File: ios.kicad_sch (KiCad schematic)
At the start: 42 parts, among them Q4 BSS138PW,115, SW1 SW_SKRPABE010, SW2 SW_SKRPABE010, SW3 SW_SKRPABE010, SW4 SW_SKRPABE010, SW8 CVS-04B, U25 74LVC06ABQ

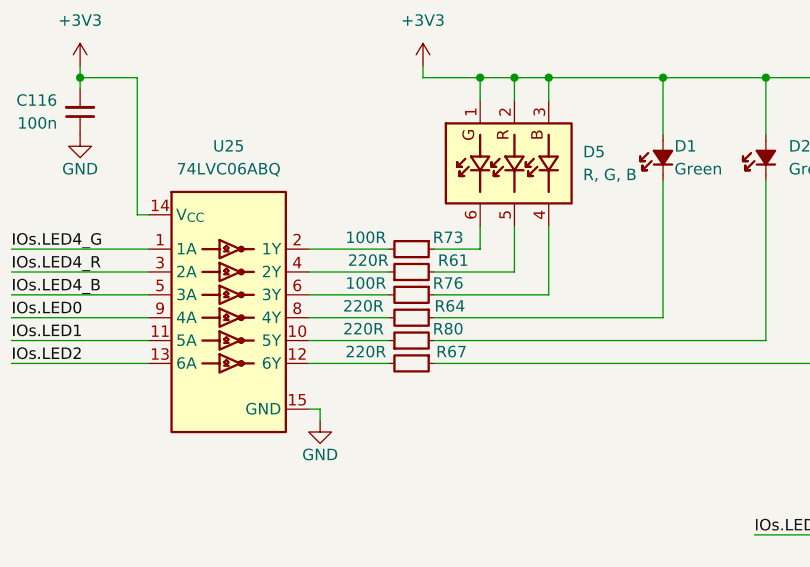
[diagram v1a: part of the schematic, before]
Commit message: [#98576] Replace RGB LED resistors with 1k
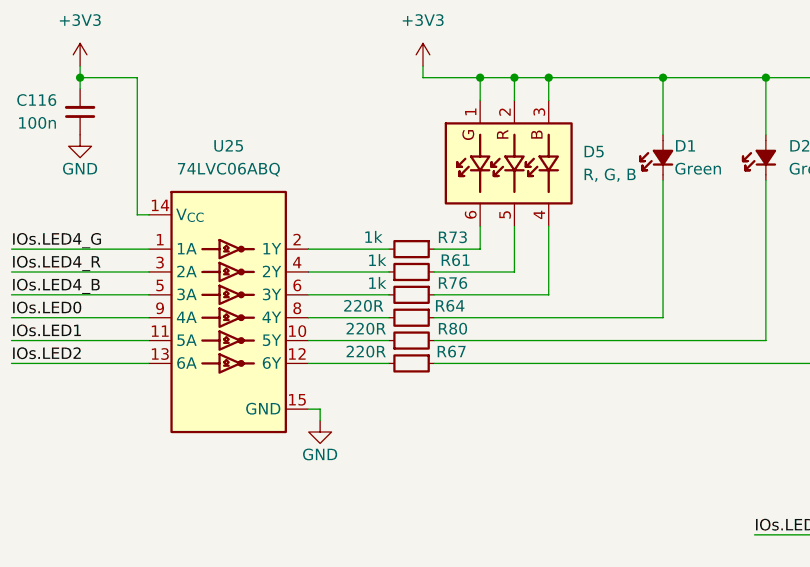
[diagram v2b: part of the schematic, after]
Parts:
- R61: value R_220R_0402 -> R_1k_0402; symbol antmicroResistors0402:R_220R_0402 -> antmicroResistors0402:R_1k_0402; MPN CR0402-FX-2200GLF -> CR0402-FX-1001GLF; Val 220R -> 1k
- R73, R76: value R_100R_0402 -> R_1k_0402; symbol antmicroResistors0402:R_100R_0402 -> antmicroResistors0402:R_1k_0402; MPN CR0402-FX-1000GLF -> CR0402-FX-1001GLF; Val 100R -> 1k
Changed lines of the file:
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@@
 	)
 	(symbol
-		(lib_id "antmicroResistors0402:R_100R_0402")
+		(lib_id "antmicroResistors0402:R_1k_0402")
 		(at 151.13 86.36 0)
 		(mirror y)
@@
 		(dnp no)
 		(property "Reference" "R73"
-			(at 152.654 85.09 0)
+			(at 153.162 85.09 0)
 			(effects
 				(font
@@
 			)
 		)
-		(property "Value" "R_100R_0402"
+		(property "Value" "R_1k_0402"
 			(at 130.81 99.06 0)
 			(effects
@@
 			)
 		)
-		(property "Description" "SMD Chip Resistor, 100 ohm, ± 1%, 62.5 mW, 0402 [1005 Metric], Thick Film, General Purpose"
+		(property "Description" "SMD Chip Resistor, 1 kohm, ± 1%, 63 mW, 0402 [1005 Metric], Thick Film, General Purpose"
 			(at 130.81 116.84 0)
 			(effects
@@
 			)
 		)
-		(property "MPN" "CR0402-FX-1000GLF"
+		(property "MPN" "CR0402-FX-1001GLF"
 			(at 130.81 106.68 0)
 			(effects
@@
 			)
 		)
-		(property "Val" "100R"
-			(at 143.51 85.09 0)
+		(property "Val" "1k"
+			(at 145.796 88.392 0)
 			(effects
 				(font
@@
 					(thickness 0.15)
 				)
+				(justify left bottom)
 			)
 		)
@@
 	)
 	(symbol
-		(lib_id "antmicroResistors0402:R_100R_0402")
+		(lib_id "antmicroResistors0402:R_1k_0402")
 		(at 151.13 91.44 0)
 		(mirror y)
@@
 		(dnp no)
 		(property "Reference" "R76"
-			(at 152.654 90.17 0)
+			(at 153.162 90.17 0)
 			(effects
 				(font
@@
 			)
 		)
-		(property "Value" "R_100R_0402"
+		(property "Value" "R_1k_0402"
 			(at 130.81 104.14 0)
 			(effects
@@
 			)
 		)
-		(property "Description" "SMD Chip Resistor, 100 ohm, ± 1%, 62.5 mW, 0402 [1005 Metric], Thick Film, General Purpose"
+		(property "Description" "SMD Chip Resistor, 1 kohm, ± 1%, 63 mW, 0402 [1005 Metric], Thick Film, General Purpose"
 			(at 130.81 121.92 0)
 			(effects
@@
 			)
 		)
-		(property "MPN" "CR0402-FX-1000GLF"
+		(property "MPN" "CR0402-FX-1001GLF"
 			(at 130.81 111.76 0)
 			(effects
@@
 			)
 		)
-		(property "Val" "100R"
-			(at 143.51 90.17 0)
+		(property "Val" "1k"
+			(at 145.796 90.932 0)
 			(effects
 				(font
@@
 					(thickness 0.15)
 				)
+				(justify left bottom)
 			)
 		)
@@
 	)
 	(symbol
-		(lib_id "antmicroResistors0402:R_220R_0402")
+		(lib_id "antmicroResistors0402:R_1k_0402")
 		(at 146.05 88.9 0)
 		(mirror x)
@@
 		(dnp no)
 		(property "Reference" "R61"
-			(at 154.94 87.63 0)
+			(at 155.194 87.63 0)
 			(effects
 				(font
@@
 			)
 		)
-		(property "Value" "R_220R_0402"
+		(property "Value" "R_1k_0402"
 			(at 166.37 76.2 0)
 			(effects
@@
 			)
 		)
-		(property "Description" "SMD Chip Resistor, 220 ohm, ± 1%, 62.5 mW, 0402 [1005 Metric], Thick Film, General Purpose"
+		(property "Description" "SMD Chip Resistor, 1 kohm, ± 1%, 63 mW, 0402 [1005 Metric], Thick Film, General Purpose"
 			(at 166.37 58.42 0)
 			(effects
@@
 			)
 		)
-		(property "MPN" "CR0402-FX-2200GLF"
+		(property "MPN" "CR0402-FX-1001GLF"
 			(at 166.37 68.58 0)
 			(effects
@@
 			)
 		)
-		(property "Val" "220R"
-			(at 146.05 87.63 0)
+		(property "Val" "1k"
+			(at 143.256 84.328 0)
 			(effects
 				(font
@@
 					(thickness 0.15)
 				)
-				(justify right)
+				(justify left bottom)
 			)
 		)
@@
 		(dnp no)
 		(property "Reference" "R80"
-			(at 152.654 95.25 0)
+			(at 153.162 95.25 0)
 			(effects
 				(font
@@
 		)
 		(property "Val" "220R"
-			(at 143.256 95.25 0)
+			(at 143.51 95.25 0)
 			(effects
 				(font

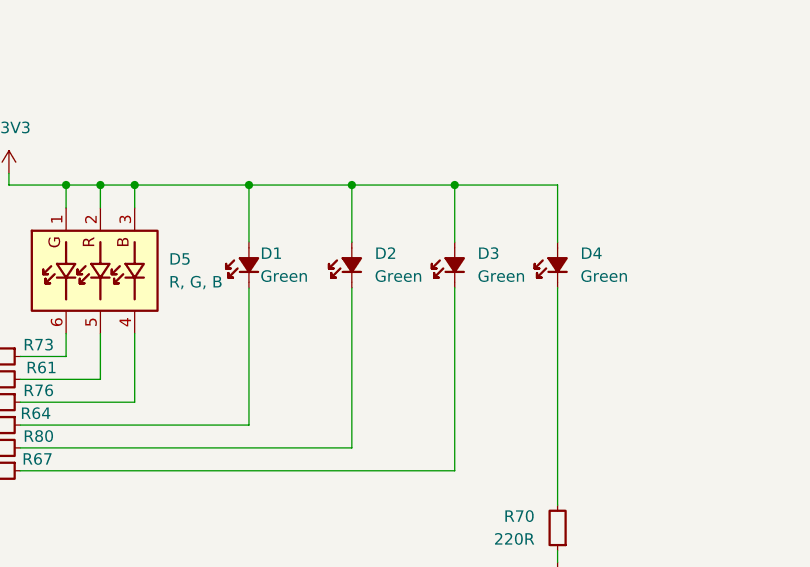
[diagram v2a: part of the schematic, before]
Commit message: [#98577] Unify LEDs
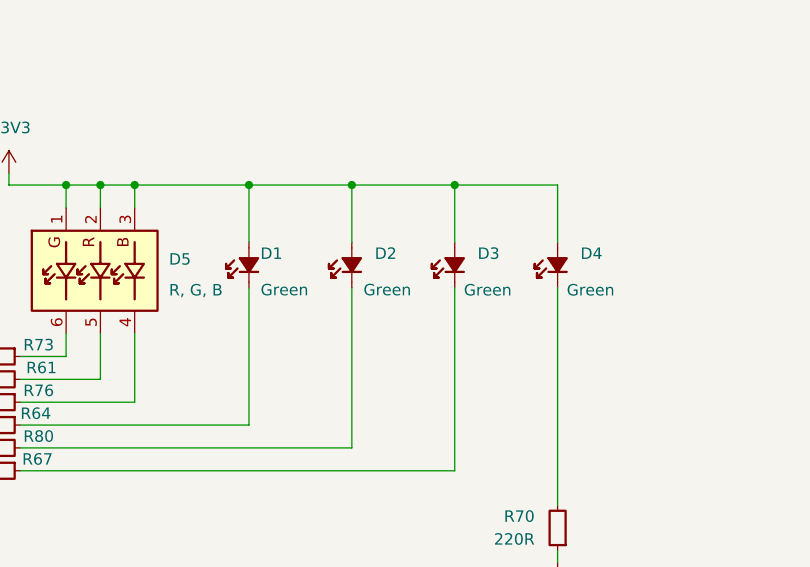
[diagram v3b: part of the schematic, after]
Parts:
- D1, D2, D3, D4: value LED_G_0402_VLMTG1500-GS08 -> LED_G_0603_LG_L29K-G2J1-24-Z; footprint antmicro-footprints:LED_0402_1005Metric_G -> antmicro-footprints:LED_0603_1608Metric_G; symbol antmicroLEDIndicationDiscrete:LED_G_0402_VLMTG1500-GS08 -> antmicroLEDIndicationDiscrete:LED_G_0603_LG_L29K-G2J1-24-Z; MPN VLMTG1500-GS08 -> LG L29K-G2J1-24-Z; Manufacturer Vishay -> OSRAM
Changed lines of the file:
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@@
 	)
 	(symbol
-		(lib_id "antmicroLEDIndicationDiscrete:LED_G_0402_VLMTG1500-GS08")
+		(lib_id "antmicroLEDIndicationDiscrete:LED_G_0603_LG_L29K-G2J1-24-Z")
 		(at 176.53 78.74 90)
 		(unit 1)
@@
 			)
 		)
-		(property "Value" "LED_G_0402_VLMTG1500-GS08"
-			(at 184.15 55.88 0)
+		(property "Value" "LED_G_0603_LG_L29K-G2J1-24-Z"
+			(at 184.15 58.42 0)
 			(effects
 				(font
@@
 			)
 		)
-		(property "Footprint" "antmicro-footprints:LED_0402_1005Metric_G"
-			(at 186.69 55.88 0)
+		(property "Footprint" "antmicro-footprints:LED_0603_1608Metric_G"
+			(at 186.69 58.42 0)
 			(effects
 				(font
@@
 			)
 		)
-		(property "Datasheet" "https://www.vishay.com/docs/82554/vlmo1500.pdf"
-			(at 189.23 55.88 0)
+		(property "Datasheet" "https://look.ams-osram.com/m/19ee86b3ae0ee95b/original/LG-L29K.pdf"
+			(at 189.23 58.42 0)
 			(effects
 				(font
@@
 			)
 		)
-		(property "Description" "LED, Green, SMD, 1005, 5 mA, 3.1 V, 535 nm"
-			(at 201.93 55.88 0)
+		(property "Description" "LED, Green, SMD, 0603, 20 mA, 1.7 V, 570 nm"
+			(at 201.93 58.42 0)
 			(effects
 				(font
@@
 			)
 		)
-		(property "MPN" "VLMTG1500-GS08"
-			(at 191.77 55.88 0)
+		(property "MPN" "LG L29K-G2J1-24-Z"
+			(at 191.77 58.42 0)
 			(effects
 				(font
@@
 			)
 		)
-		(property "Manufacturer" "Vishay"
-			(at 194.31 55.88 0)
+		(property "Manufacturer" "OSRAM"
+			(at 194.31 58.42 0)
 			(effects
 				(font
@@
 		)
 		(property "Color" "Green"
-			(at 177.8 77.4699 90)
+			(at 183.134 78.232 90)
 			(effects
 				(font
 					(size 1.27 1.27)
 				)
-				(justify right)
+				(justify left bottom)
 			)
 		)
 		(property "Author" "Antmicro"
-			(at 196.85 55.88 0)
+			(at 196.85 58.42 0)
 			(effects
 				(font
@@
 		)
 		(property "License" "Apache-2.0"
-			(at 199.39 55.88 0)
+			(at 199.39 58.42 0)
 			(effects
 				(font
@@
 	)
 	(symbol
-		(lib_id "antmicroLEDIndicationDiscrete:LED_G_0402_VLMTG1500-GS08")
+		(lib_id "antmicroLEDIndicationDiscrete:LED_G_0603_LG_L29K-G2J1-24-Z")
 		(at 199.39 78.74 90)
 		(unit 1)
@@
 		(on_board yes)
 		(dnp no)
-		(fields_autoplaced yes)
 		(property "Reference" "D3"
 			(at 201.93 74.93 90)
@@
 			)
 		)
-		(property "Value" "LED_G_0402_VLMTG1500-GS08"
-			(at 207.01 55.88 0)
+		(property "Value" "LED_G_0603_LG_L29K-G2J1-24-Z"
+			(at 207.01 58.42 0)
 			(effects
 				(font
@@
 			)
 		)
-		(property "Footprint" "antmicro-footprints:LED_0402_1005Metric_G"
-			(at 209.55 55.88 0)
+		(property "Footprint" "antmicro-footprints:LED_0603_1608Metric_G"
+			(at 209.55 58.42 0)
 			(effects
 				(font
@@
 			)
 		)
-		(property "Datasheet" "https://www.vishay.com/docs/82554/vlmo1500.pdf"
-			(at 212.09 55.88 0)
+		(property "Datasheet" "https://look.ams-osram.com/m/19ee86b3ae0ee95b/original/LG-L29K.pdf"
+			(at 212.09 58.42 0)
 			(effects
 				(font
@@
 			)
 		)
-		(property "Description" "LED, Green, SMD, 1005, 5 mA, 3.1 V, 535 nm"
-			(at 224.79 55.88 0)
+		(property "Description" "LED, Green, SMD, 0603, 20 mA, 1.7 V, 570 nm"
+			(at 224.79 58.42 0)
 			(effects
 				(font
@@
 			)
 		)
-		(property "MPN" "VLMTG1500-GS08"
-			(at 214.63 55.88 0)
+		(property "MPN" "LG L29K-G2J1-24-Z"
+			(at 214.63 58.42 0)
 			(effects
 				(font
@@
 			)
 		)
-		(property "Manufacturer" "Vishay"
-			(at 217.17 55.88 0)
+		(property "Manufacturer" "OSRAM"
+			(at 217.17 58.42 0)
 			(effects
 				(font
@@
 		)
 		(property "Color" "Green"
-			(at 201.93 77.4699 90)
+			(at 200.406 78.994 90)
 			(effects
 				(font
@@
 		)
 		(property "Author" "Antmicro"
-			(at 219.71 55.88 0)
+			(at 219.71 58.42 0)
 			(effects
 				(font
@@
 		)
 		(property "License" "Apache-2.0"
-			(at 222.25 55.88 0)
+			(at 222.25 58.42 0)
 			(effects
 				(font
@@
 	)
 	(symbol
-		(lib_id "antmicroLEDIndicationDiscrete:LED_G_0402_VLMTG1500-GS08")
+		(lib_id "antmicroLEDIndicationDiscrete:LED_G_0603_LG_L29K-G2J1-24-Z")
 		(at 187.96 78.74 90)
 		(unit 1)
@@
 			)
 		)
-		(property "Value" "LED_G_0402_VLMTG1500-GS08"
-			(at 195.58 55.88 0)
+		(property "Value" "LED_G_0603_LG_L29K-G2J1-24-Z"
+			(at 195.58 58.42 0)
 			(effects
 				(font
@@
 			)
 		)
-		(property "Footprint" "antmicro-footprints:LED_0402_1005Metric_G"
-			(at 198.12 55.88 0)
+		(property "Footprint" "antmicro-footprints:LED_0603_1608Metric_G"
+			(at 198.12 58.42 0)
 			(effects
 				(font
@@
 			)
 		)
-		(property "Datasheet" "https://www.vishay.com/docs/82554/vlmo1500.pdf"
-			(at 200.66 55.88 0)
+		(property "Datasheet" "https://look.ams-osram.com/m/19ee86b3ae0ee95b/original/LG-L29K.pdf"
+			(at 200.66 58.42 0)
 			(effects
 				(font
@@
 			)
 		)
-		(property "Description" "LED, Green, SMD, 1005, 5 mA, 3.1 V, 535 nm"
-			(at 213.36 55.88 0)
+		(property "Description" "LED, Green, SMD, 0603, 20 mA, 1.7 V, 570 nm"
+			(at 213.36 58.42 0)
 			(effects
 				(font
@@
 			)
 		)
-		(property "MPN" "VLMTG1500-GS08"
-			(at 203.2 55.88 0)
+		(property "MPN" "LG L29K-G2J1-24-Z"
+			(at 203.2 58.42 0)
 			(effects
 				(font
@@
 			)
 		)
-		(property "Manufacturer" "Vishay"
-			(at 205.74 55.88 0)
+		(property "Manufacturer" "OSRAM"
+			(at 205.74 58.42 0)
 			(effects
 				(font
@@
 		)
 		(property "Color" "Green"
-			(at 190.5 77.4699 90)
+			(at 194.564 78.232 90)
 			(effects
 				(font
 					(size 1.27 1.27)
 				)
-				(justify right)
+				(justify left bottom)
 			)
 		)
 		(property "Author" "Antmicro"
-			(at 208.28 55.88 0)
+			(at 208.28 58.42 0)
 			(effects
 				(font
@@
 		)
 		(property "License" "Apache-2.0"
-			(at 210.82 55.88 0)
+			(at 210.82 58.42 0)
 			(effects
 				(font
@@
 		(on_board yes)
 		(dnp no)
-		(fields_autoplaced yes)
 		(property "Reference" "D5"
 			(at 167.64 75.565 90)
@@
 		)
 		(property "Color" "R, G, B"
-			(at 167.64 78.1049 90)
+			(at 167.64 78.994 90)
 			(effects
 				(font
@@
 	)
 	(symbol
-		(lib_id "antmicroLEDIndicationDiscrete:LED_G_0402_VLMTG1500-GS08")
+		(lib_id "antmicroLEDIndicationDiscrete:LED_G_0603_LG_L29K-G2J1-24-Z")
 		(at 210.82 78.74 90)
 		(unit 1)
@@
 		(on_board yes)
 		(dnp no)
-		(fields_autoplaced yes)
 		(property "Reference" "D4"
 			(at 213.36 74.93 90)
@@
 			)
 		)
-		(property "Value" "LED_G_0402_VLMTG1500-GS08"
-			(at 218.44 55.88 0)
+		(property "Value" "LED_G_0603_LG_L29K-G2J1-24-Z"
+			(at 218.44 58.42 0)
 			(effects
 				(font
@@
 			)
 		)
-		(property "Footprint" "antmicro-footprints:LED_0402_1005Metric_G"
-			(at 220.98 55.88 0)
+		(property "Footprint" "antmicro-footprints:LED_0603_1608Metric_G"
+			(at 220.98 58.42 0)
 			(effects
 				(font
@@
 			)
 		)
-		(property "Datasheet" "https://www.vishay.com/docs/82554/vlmo1500.pdf"
-			(at 223.52 55.88 0)
+		(property "Datasheet" "https://look.ams-osram.com/m/19ee86b3ae0ee95b/original/LG-L29K.pdf"
+			(at 223.52 58.42 0)
 			(effects
 				(font
@@
 			)
 		)
-		(property "Description" "LED, Green, SMD, 1005, 5 mA, 3.1 V, 535 nm"
-			(at 236.22 55.88 0)
+		(property "Description" "LED, Green, SMD, 0603, 20 mA, 1.7 V, 570 nm"
+			(at 236.22 58.42 0)
 			(effects
 				(font
@@
 			)
 		)
-		(property "MPN" "VLMTG1500-GS08"
-			(at 226.06 55.88 0)
+		(property "MPN" "LG L29K-G2J1-24-Z"
+			(at 226.06 58.42 0)
 			(effects
 				(font
@@
 			)
 		)
-		(property "Manufacturer" "Vishay"
-			(at 228.6 55.88 0)
+		(property "Manufacturer" "OSRAM"
+			(at 228.6 58.42 0)
 			(effects
 				(font
@@
 		)
 		(property "Color" "Green"
-			(at 213.36 77.4699 90)
+			(at 211.836 78.994 90)
 			(effects
 				(font
@@
 		)
 		(property "Author" "Antmicro"
-			(at 231.14 55.88 0)
+			(at 231.14 58.42 0)
 			(effects
 				(font
@@
 		)
 		(property "License" "Apache-2.0"
-			(at 233.68 55.88 0)
+			(at 233.68 58.42 0)
 			(effects
 				(font

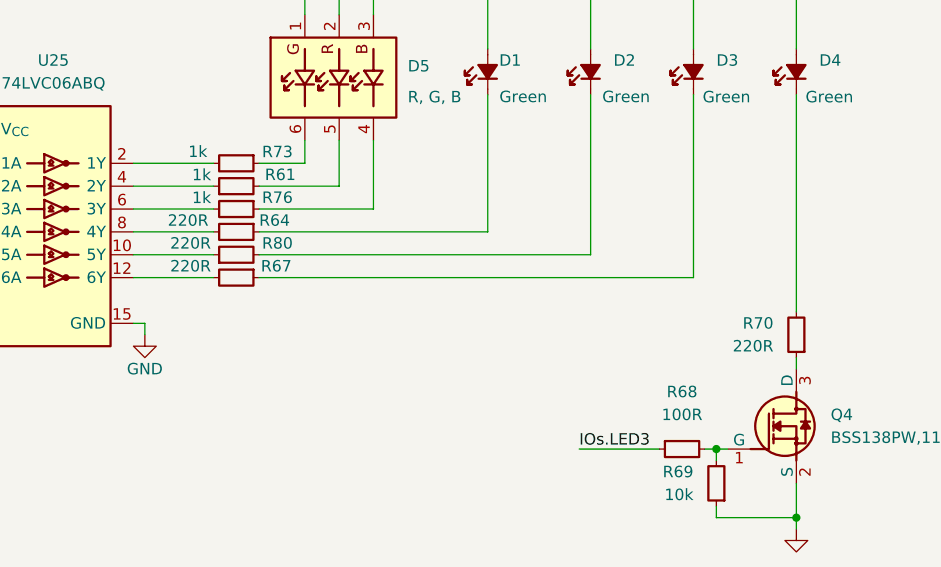
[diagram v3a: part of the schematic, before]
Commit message: [#98577] Unify LED Resistor values
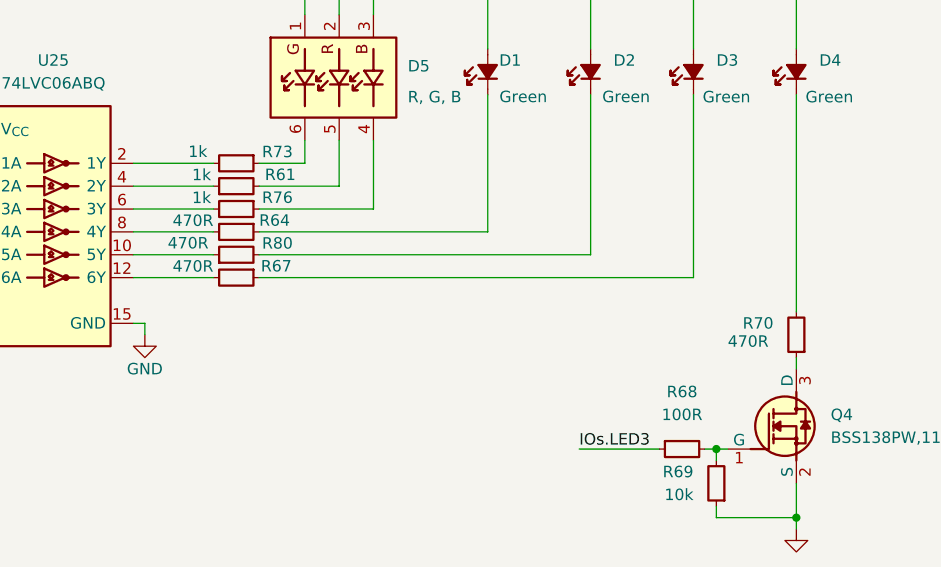
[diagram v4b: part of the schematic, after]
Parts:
- R64, R67, R70, R80: value R_220R_0402 -> R_470R_0402; symbol antmicroResistors0402:R_220R_0402 -> antmicroResistors0402:R_470R_0402; MPN CR0402-FX-2200GLF -> CR0402-FX-4700GLF; Val 220R -> 470R
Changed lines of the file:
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@@
 	)
 	(symbol
-		(lib_id "antmicroResistors0402:R_220R_0402")
+		(lib_id "antmicroResistors0402:R_470R_0402")
 		(at 210.82 107.95 270)
 		(mirror x)
@@
 			)
 		)
-		(property "Value" "R_220R_0402"
+		(property "Value" "R_470R_0402"
 			(at 198.12 87.63 0)
 			(effects
@@
 			)
 		)
-		(property "Description" "SMD Chip Resistor, 220 ohm, ± 1%, 62.5 mW, 0402 [1005 Metric], Thick Film, General Purpose"
+		(property "Description" "SMD Chip Resistor, 470 ohm, ± 1%, 62.5 mW, 0402 [1005 Metric], Thick Film, General Purpose"
 			(at 180.34 87.63 0)
 			(effects
@@
 			)
 		)
-		(property "MPN" "CR0402-FX-2200GLF"
+		(property "MPN" "CR0402-FX-4700GLF"
 			(at 190.5 87.63 0)
 			(effects
@@
 			)
 		)
-		(property "Val" "220R"
-			(at 208.28 106.68 90)
+		(property "Val" "470R"
+			(at 203.2 105.41 90)
 			(effects
 				(font
@@
 					(thickness 0.15)
 				)
-				(justify right)
+				(justify left bottom)
 			)
 		)
@@
 	)
 	(symbol
-		(lib_id "antmicroResistors0402:R_220R_0402")
+		(lib_id "antmicroResistors0402:R_470R_0402")
 		(at 151.13 93.98 0)
 		(mirror y)
@@
 			)
 		)
-		(property "Value" "R_220R_0402"
+		(property "Value" "R_470R_0402"
 			(at 130.81 106.68 0)
 			(effects
@@
 			)
 		)
-		(property "Description" "SMD Chip Resistor, 220 ohm, ± 1%, 62.5 mW, 0402 [1005 Metric], Thick Film, General Purpose"
+		(property "Description" "SMD Chip Resistor, 470 ohm, ± 1%, 62.5 mW, 0402 [1005 Metric], Thick Film, General Purpose"
 			(at 130.81 124.46 0)
 			(effects
@@
 			)
 		)
-		(property "MPN" "CR0402-FX-2200GLF"
+		(property "MPN" "CR0402-FX-4700GLF"
 			(at 130.81 114.3 0)
 			(effects
@@
 			)
 		)
-		(property "Val" "220R"
-			(at 140.97 92.71 0)
+		(property "Val" "470R"
+			(at 146.05 93.472 0)
 			(effects
 				(font
@@
 					(thickness 0.15)
 				)
-				(justify right)
+				(justify left bottom)
 			)
 		)
@@
 	)
 	(symbol
-		(lib_id "antmicroResistors0402:R_220R_0402")
+		(lib_id "antmicroResistors0402:R_470R_0402")
 		(at 151.13 99.06 0)
 		(mirror y)
@@
 			)
 		)
-		(property "Value" "R_220R_0402"
+		(property "Value" "R_470R_0402"
 			(at 130.81 111.76 0)
 			(effects
@@
 			)
 		)
-		(property "Description" "SMD Chip Resistor, 220 ohm, ± 1%, 62.5 mW, 0402 [1005 Metric], Thick Film, General Purpose"
+		(property "Description" "SMD Chip Resistor, 470 ohm, ± 1%, 62.5 mW, 0402 [1005 Metric], Thick Film, General Purpose"
 			(at 130.81 129.54 0)
 			(effects
@@
 			)
 		)
-		(property "MPN" "CR0402-FX-2200GLF"
+		(property "MPN" "CR0402-FX-4700GLF"
 			(at 130.81 119.38 0)
 			(effects
@@
 			)
 		)
-		(property "Val" "220R"
-			(at 143.51 97.79 0)
+		(property "Val" "470R"
+			(at 146.05 98.552 0)
 			(effects
 				(font
@@
 					(thickness 0.15)
 				)
+				(justify left bottom)
 			)
 		)
@@
 	)
 	(symbol
-		(lib_id "antmicroResistors0402:R_220R_0402")
+		(lib_id "antmicroResistors0402:R_470R_0402")
 		(at 146.05 96.52 0)
 		(mirror x)
@@
 			)
 		)
-		(property "Value" "R_220R_0402"
+		(property "Value" "R_470R_0402"
 			(at 166.37 83.82 0)
 			(effects
@@
 			)
 		)
-		(property "Description" "SMD Chip Resistor, 220 ohm, ± 1%, 62.5 mW, 0402 [1005 Metric], Thick Film, General Purpose"
+		(property "Description" "SMD Chip Resistor, 470 ohm, ± 1%, 62.5 mW, 0402 [1005 Metric], Thick Film, General Purpose"
 			(at 166.37 66.04 0)
 			(effects
@@
 			)
 		)
-		(property "MPN" "CR0402-FX-2200GLF"
+		(property "MPN" "CR0402-FX-4700GLF"
 			(at 166.37 76.2 0)
 			(effects
@@
 			)
 		)
-		(property "Val" "220R"
-			(at 143.51 95.25 0)
+		(property "Val" "470R"
+			(at 140.97 94.488 0)
 			(effects
 				(font
@@
 					(thickness 0.15)
 				)
+				(justify left bottom)
 			)
 		)
